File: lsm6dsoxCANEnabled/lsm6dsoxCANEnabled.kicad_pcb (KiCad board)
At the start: 2 copper layers, 49.1 x 46.7 mm, 29 parts, among them J1 CANH and CANL, J2 GPIO, J3 Power, SW1 Nrst, SW2 BOOT0 selector, U2 TJA1051T, U3 STM32F103C8Tx, U4 AMS1117CD-3.3, Y1 Crystal_GND24

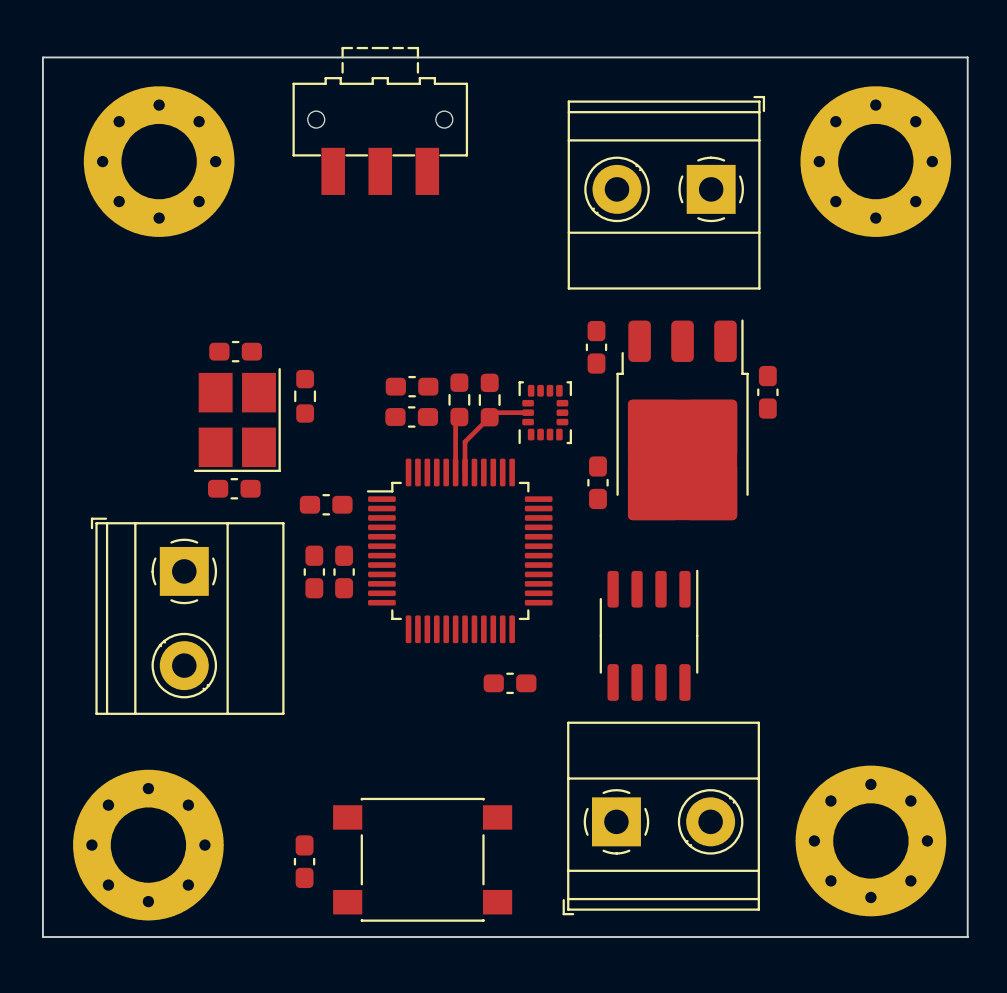
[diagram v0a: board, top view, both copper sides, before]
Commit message: Started pcb with component placement and physical size constraints
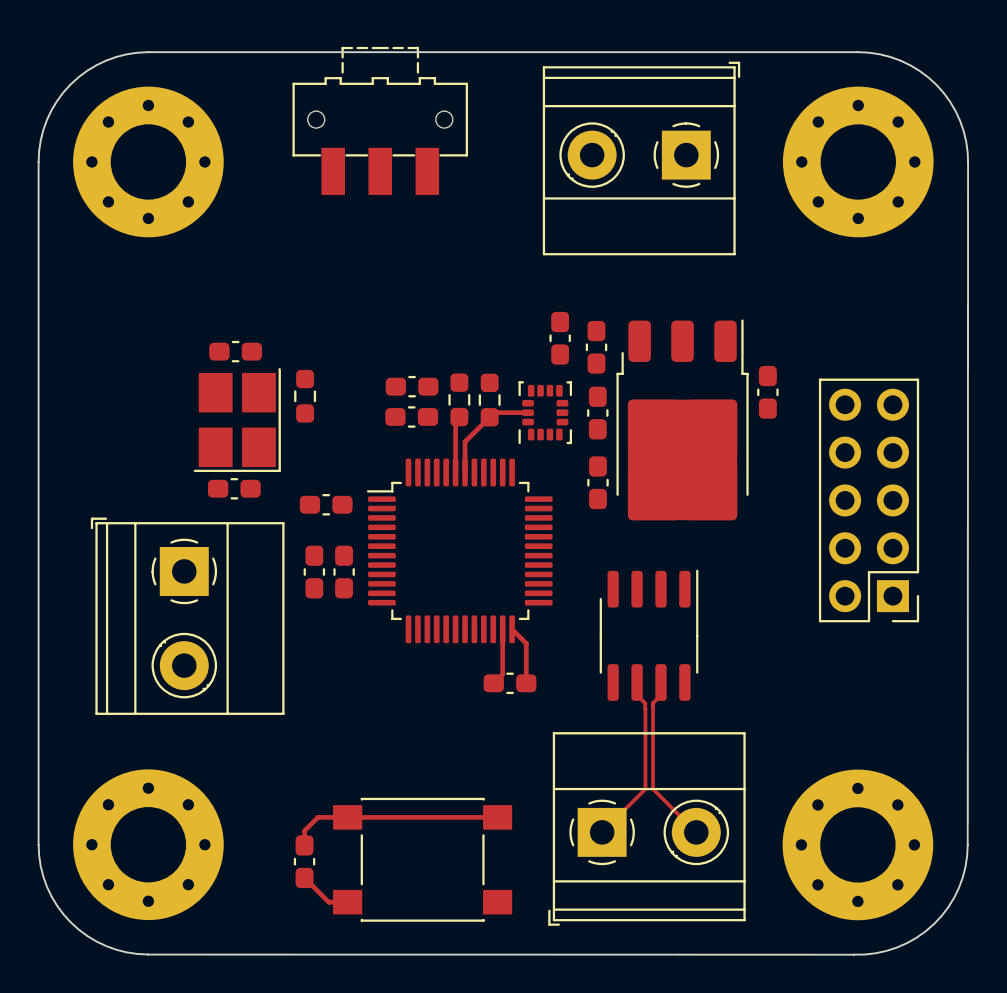
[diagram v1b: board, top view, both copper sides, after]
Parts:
- added C13: 100n, Capacitor_SMD:C_0603_1608Metric_Pad1.08x0.95mm_HandSolder, F.Cu at (142.0, 80.0)
- added C14: 100n, Capacitor_SMD:C_0603_1608Metric_Pad1.08x0.95mm_HandSolder, F.Cu at (140.0, 76.0)
- added J4: SWD, Connector_PinHeader_2.54mm:PinHeader_2x05_P2.54mm_Vertical, F.Cu at (157.7, 89.7)
- R1, R2: value 2k2 -> 10k
- moved J3 2.25 mm to (146.7, 66.3)
- moved J1 0.94 mm to (142.2, 102.2)
- moved H3 0.93 mm to (155.8, 66.7)
- moved H4 0.72 mm to (155.8, 102.9)
- moved H1 0.57 mm to (118.2, 66.7)
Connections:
- net Net-(J1-Pin_1) renamed CAN-
- net Net-(J1-Pin_2) renamed CAN+
- U1 pad 1: unconnected-(U1-SD0-Pad1) -> SDO
- U1 pad 12: unconnected-(U1-CS-Pad12) -> CS
- U1 pad 2: unconnected-(U1-SDX-Pad2) -> GND
- U1 pad 3: unconnected-(U1-SCX-Pad3) -> GND
- U3 pad 16: unconnected-(U3-PA6-Pad16) -> SDO
- U3 pad 18: unconnected-(U3-PB0-Pad18) -> CS
- U3 pad 32: unconnected-(U3-PA11-Pad32) -> CAN_RX
- U3 pad 34: CAN_RX -> SYS_JTMS_SWDIO
- U3 pad 37: unconnected-(U3-PA14-Pad37) -> SYS_JTCK_SWCL
- U3 pad 39: unconnected-(U3-PB3-Pad39) -> SYS_JTDO_TRACESWO
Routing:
- net NRST: track 0.00 -> 11.3 mm
- net CAN+: track 0.00 -> 9.10 mm
- net CAN-: track 0.00 -> 9.10 mm
- net +3.3V: track 0.00 -> 3.18 mm
- net GND: track 0.00 -> 3.06 mm
- net Net-(C1-Pad2): track 0.00 -> 2.82 mm
- added copper zone on In1.Cu, net +3.3V
- added copper zone on In2.Cu, net GND
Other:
- board size 49.1 x 46.7 mm -> 49.3 x 47.9 mm
- copper layers 2 -> 4

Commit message: started the routing process for the CAN LSM6DSOX
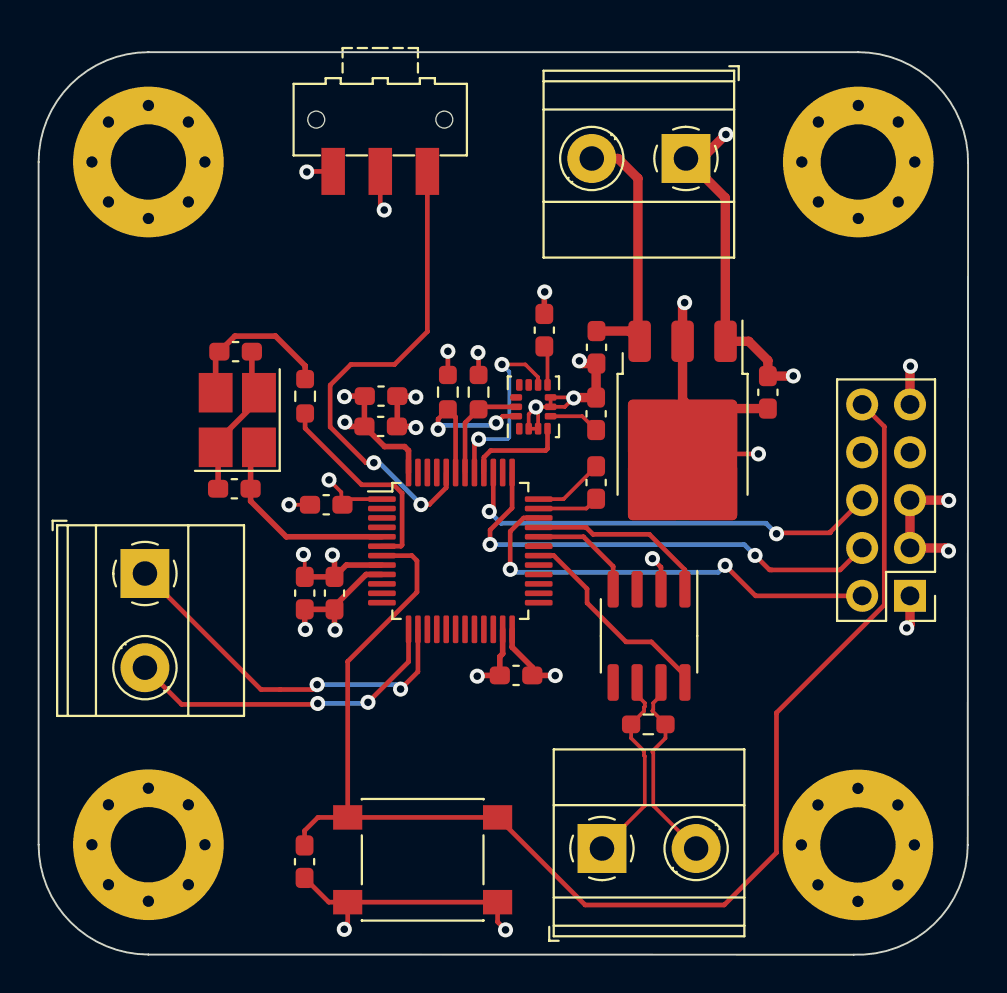
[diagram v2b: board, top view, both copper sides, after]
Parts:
- added R4: 120, Resistor_SMD:R_0603_1608Metric_Pad0.98x0.95mm_HandSolder, F.Cu at (144.7, 96.5)
- moved J2 2.09 mm to (118.0, 88.5)
- moved C10 1.72 mm to (130.5, 79.1)
- moved C7 1.72 mm to (130.5, 80.7)
- moved C11 1.23 mm to (128.0, 89.5)
- moved C12 1.23 mm to (126.5, 89.5)
- moved C14 0.94 mm to (139.2, 75.6)
- moved J4 0.91 mm to (158.6, 89.7)
- moved J1 0.86 mm to (142.2, 103.1)
- moved R2 0.73 mm to (134.1, 78.9)
- moved R1 0.72 mm to (135.7, 78.9)
- moved U1 0.70 mm to (138.6, 79.7)
- moved C9 0.53 mm to (137.7, 93.9)
- moved J3 0.18 mm to (146.7, 66.5)
- moved C8 0.10 mm to (141.9, 83.7)
- moved C13 0.10 mm to (141.9, 80.0), turned to 90 degrees
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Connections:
- C1 pad 2: Net-(C1-Pad2) -> GND
- SW1 pad 1: Net-(C1-Pad2) -> GND
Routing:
- net GND: track 3.06 -> 83.8 mm, vias 0 -> 19
- net NRST: track 11.3 -> 73.0 mm
- net +3.3V: track 3.18 -> 53.1 mm, vias 0 -> 12
- net BOOT0: track 0.00 -> 26.2 mm, vias 0 -> 2
- net SYS_JTCK_SWCL: track 0.00 -> 25.1 mm, vias 0 -> 2
- net SYS_JTMS_SWDIO: track 0.00 -> 23.4 mm, vias 0 -> 2
- net SYS_JTDO_TRACESWO: track 0.00 -> 23.2 mm, vias 0 -> 2
- net GPIO2: track 0.00 -> 19.9 mm, vias 0 -> 2
- net GPIO1: track 0.00 -> 17.5 mm, vias 0 -> 2
- net +5V: track 0.00 -> 14.1 mm
- net HSE_OUT: track 0.00 -> 11.2 mm
- net Silent_Mode: track 0.00 -> 11.2 mm
- net HSE_In: track 0.00 -> 10.8 mm
- net INT2: track 0.00 -> 10.2 mm, vias 0 -> 2
- net CAN_TX: track 0.00 -> 9.73 mm
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
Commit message: almost finished routing just need to solve clearance issues and route 5V with a potential power plane
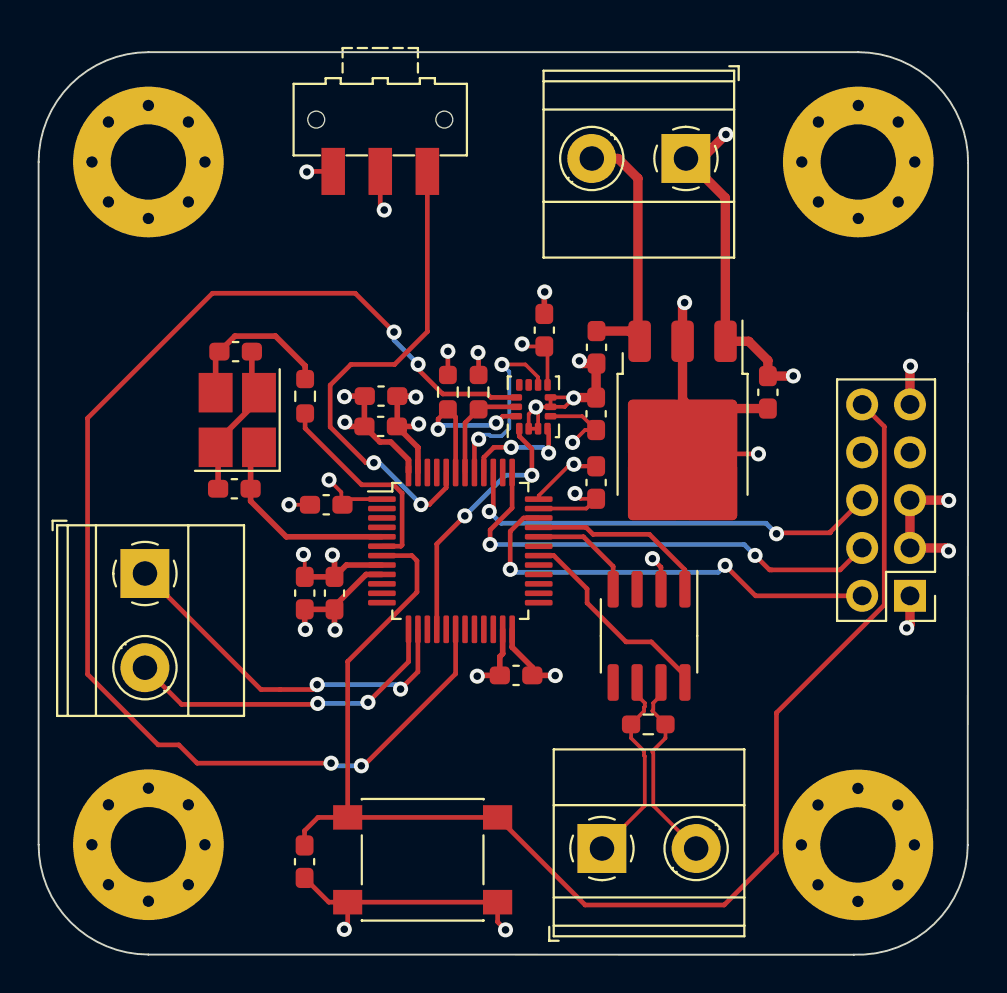
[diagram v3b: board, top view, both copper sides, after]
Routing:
- net CS: track 0.00 -> 67.7 mm, vias 0 -> 4
- net SDO: track 0.00 -> 13.8 mm, vias 0 -> 2
- net GND: track 83.8 -> 88.1 mm, vias 19 -> 20
- net +3.3V: track 53.1 -> 57.3 mm, vias 12 -> 15
- net INT1: track 5.43 -> 5.90 mm, vias 0 -> 2

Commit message: decided to connect 5V connections directly instead of making a power plane. Probably should change this later
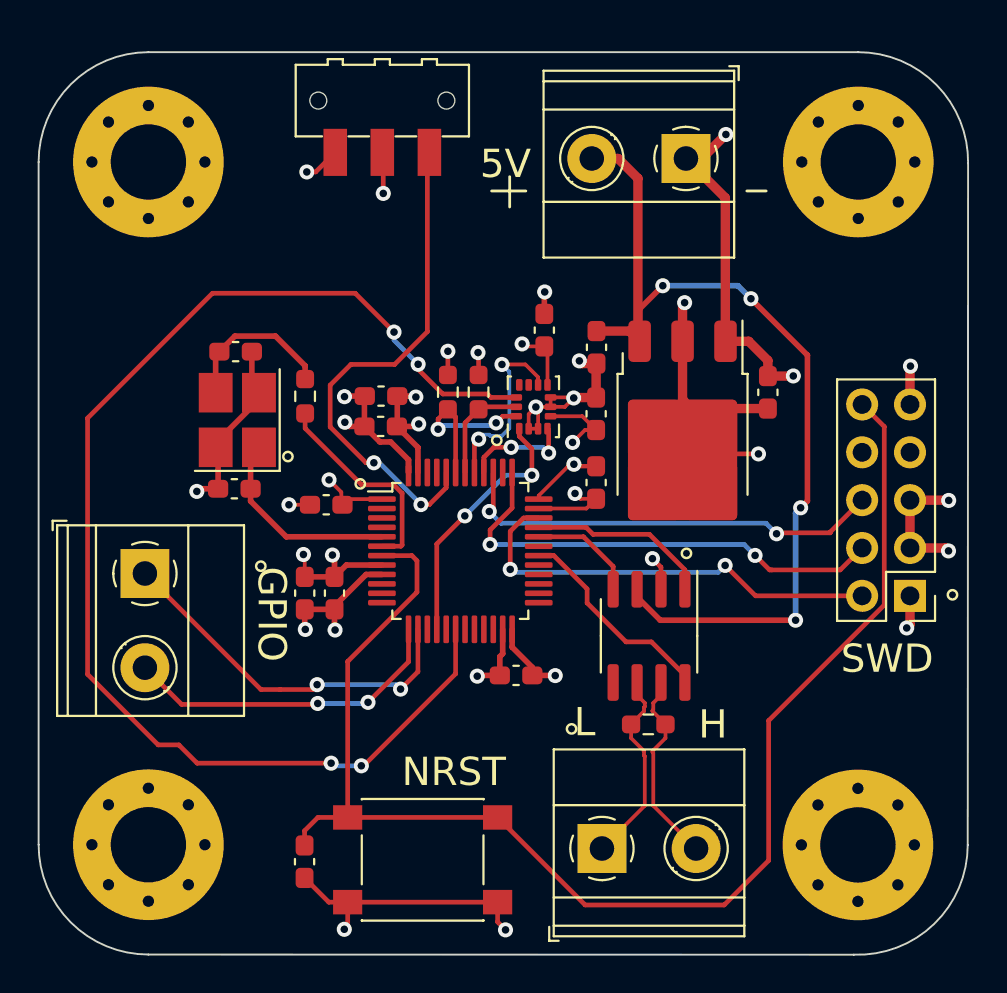
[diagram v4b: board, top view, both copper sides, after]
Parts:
- moved SW2 1.02 mm to (130.6, 63.4)
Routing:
- net +5V: track 14.1 -> 50.4 mm, vias 0 -> 4
- net GND: track 88.1 -> 89.9 mm, vias 20 -> 21
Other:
- board text added: "5V"
- board text added: "GPIO"
- board text added: "H"
- board text added: "L"
- board text added: "NRST"
- board text added: "SWD"

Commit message: moved SWD to the left side divided the power plane between 3.3 and 5v and did some rerouting of traces
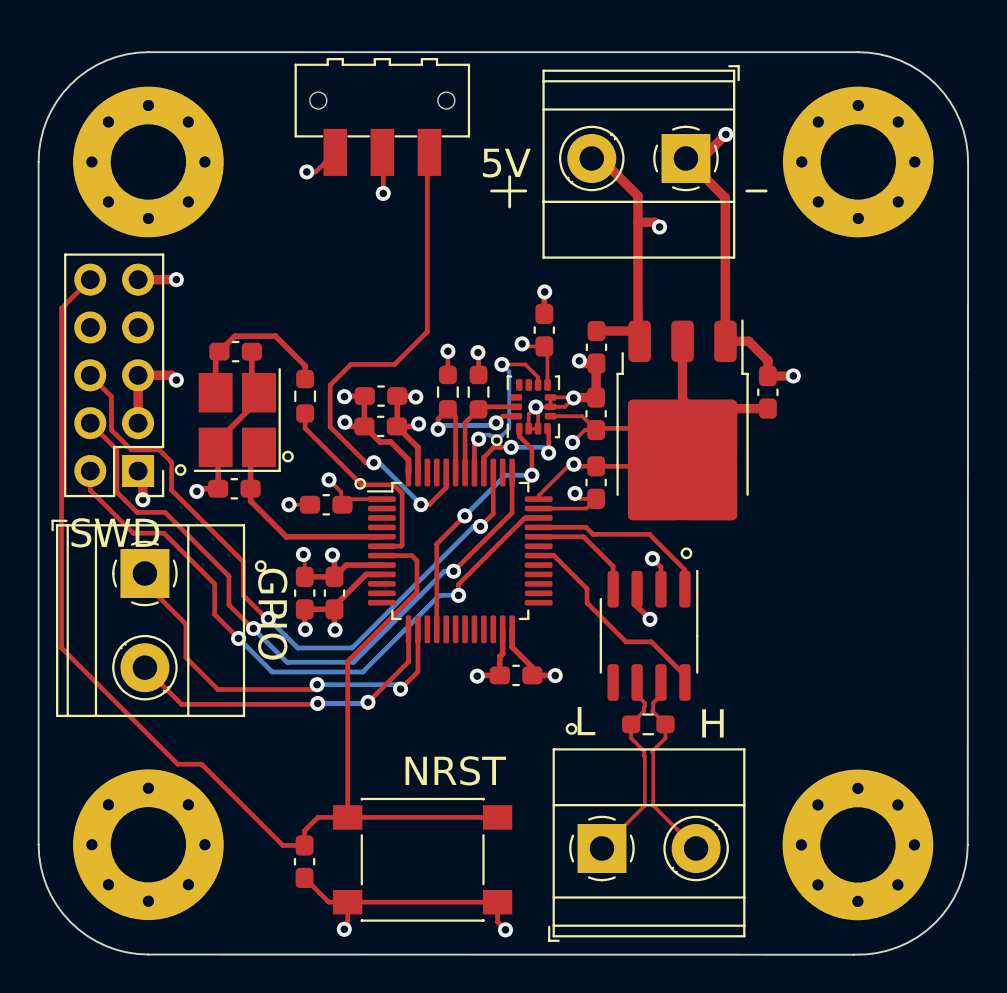
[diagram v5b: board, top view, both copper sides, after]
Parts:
- moved J4 41.5 mm to (117.6, 83.1)
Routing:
- net CS: track 67.7 -> 0.00 mm, vias 4 -> 0
- net +5V: track 50.4 -> 18.8 mm, vias 4 -> 2
- net SYS_JTDO_TRACESWO: track 23.2 -> 35.5 mm
- net SYS_JTCK_SWCL: track 25.1 -> 35.3 mm
- net SYS_JTMS_SWDIO: track 23.4 -> 33.5 mm
- net NRST: track 73.0 -> 65.9 mm
- net GND: track 89.9 -> 87.8 mm, vias 21 -> 20
- net GPIO2: track 19.9 -> 21.2 mm
- net +3.3V: track 57.3 -> 58.1 mm, vias 15 -> 13
- added copper zone on In1.Cu, net +5V

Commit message: added DFR logo,revision number, and the current date
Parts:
- added D1: LED, LED_SMD:LED_0603_1608Metric_Pad1.05x0.95mm_HandSolder, F.Cu at (160.0, 73.4)
- added G***: LOGO, LOGO, B.Cu at (135.5, 82.7)
- added R5: 2k2, Resistor_SMD:R_0603_1608Metric_Pad0.98x0.95mm_HandSolder, F.Cu at (157.4, 72.5)
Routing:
- net +3.3V: track 58.1 -> 69.3 mm
- net Net-(D1-K): track 0.00 -> 1.80 mm
- net GND: track 87.8 -> 89.0 mm, vias 20 -> 21
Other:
- board text added: "2/5/24"
- board text added: "Rev 1"

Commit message: updated some stuff
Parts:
- removed J1: CANH and CANL, TerminalBlock_Phoenix:TerminalBlock_Phoenix_MKDS-1,5-2_1x02_P5.00mm_Horizontal
- added G***: LOGO, LOGO, B.Cu at (155.7, 89.3)
- added J5: CANH and CANL input n output, TerminalBlock_Phoenix:TerminalBlock_Phoenix_MKDS-1,5-4_1x04_P5.00mm_Horizontal, F.Cu at (132.1, 103.3)
- SW2: value BOOT0 selector -> BOOT0
- moved C1 29.3 mm to (154.5, 95.2), turned to 0 degrees
- moved SW1 26.2 mm to (154.4, 88.9), turned to -90 degrees
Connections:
- SW2 pad 1: BOOT0 -> +3.3V
- SW2 pad 2: +3.3V -> BOOT0
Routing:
- net CS: track 0.00 -> 61.8 mm, vias 0 -> 4
- net NRST: track 65.9 -> 88.7 mm, vias 0 -> 2
- net CAN+: track 10.5 -> 31.8 mm
- net CAN-: track 10.5 -> 30.5 mm
- net +5V: track 18.8 -> 17.2 mm
- net GND: track 89.0 -> 90.3 mm, vias 21 -> 22
- net BOOT0: track 26.2 -> 24.9 mm
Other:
- board text added: "BootL"
- board text added: "CAN"
- board text added: "Flash"

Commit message: added finishing touches to the rev 2 design
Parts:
- added J1: Termination Resistor, Connector_PinHeader_2.54mm:PinHeader_1x02_P2.54mm_Vertical, F.Cu at (125.2, 102.1)
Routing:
- net CAN-: track 30.5 -> 48.1 mm
- net CAN+: track 31.8 -> 48.8 mm
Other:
- board text added: "Term"
